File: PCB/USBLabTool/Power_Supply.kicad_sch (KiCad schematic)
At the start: 53 parts, among them J19 T_N5V, U10 Opamp_Quad, U11 DG403, U13 r1283, U15 ST1L05APU33R, U16 LTC1983ES6-5#TRPBF, U19 ST1L05APU33R, U9 Opamp_Quad

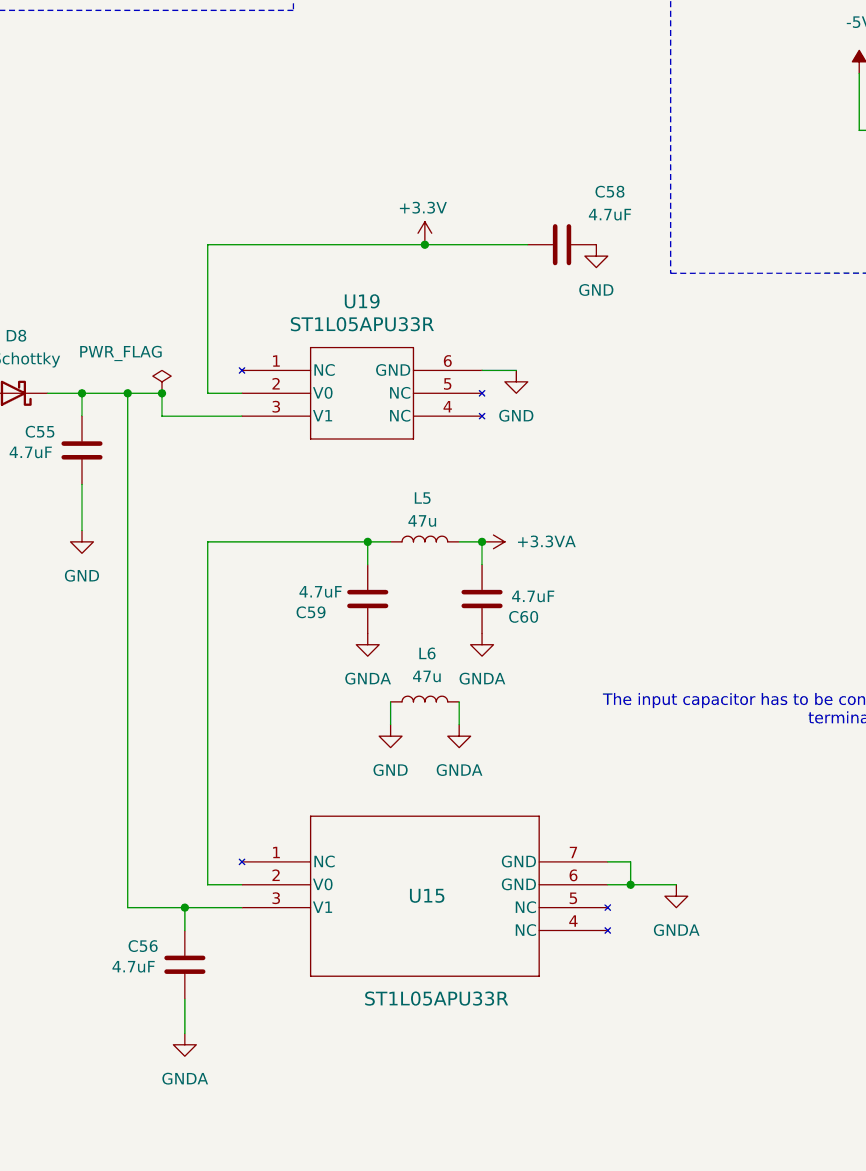
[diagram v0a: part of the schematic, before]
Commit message: update ST1L05APU33R schematic
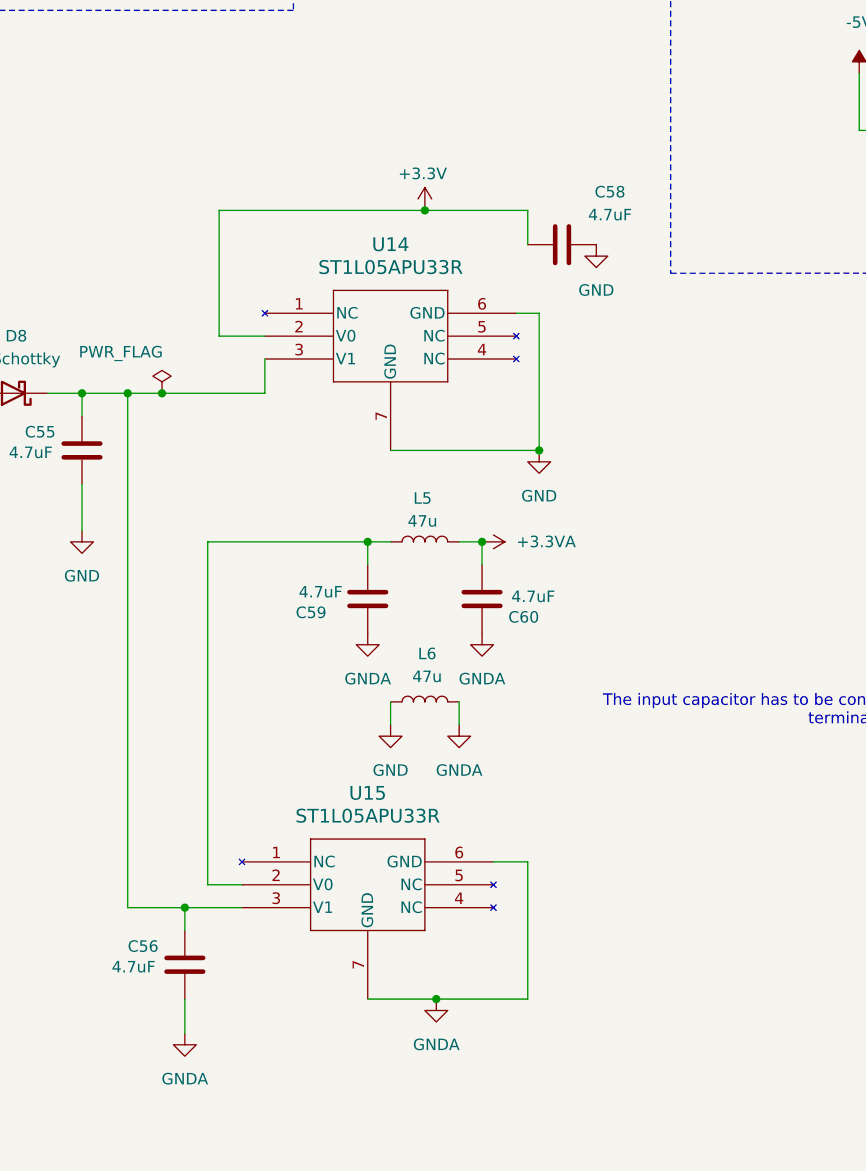
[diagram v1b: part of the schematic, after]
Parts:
- removed U15: ST1L05APU33R, DFN_5APU33R_STM, symbol ST1L05APU33R:ST1L05APU33R
- removed U19: ST1L05APU33R, DFN_5APU33R_STM, symbol USBLabTool:ST1L05APU33R
- added U14, U15: ST1L05APU33R, DFN_5APU33R_STM, symbol USBLabTool:ST1L05APU33R
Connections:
- net +3.3V: now also U14.2 (V0)
- net GND: now also U14.6 (GND), U14.7 (GND)
- net GNDA: now also U15.6 (GND), U15.7 (GND)
- net at C59.2, L5.1: now also U15.2 (V0)
- net at C55.1, C56.1, D8.1 (K): now also U14.3 (V1), U15.3 (V1)

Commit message: continue PCB layout
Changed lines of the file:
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@@
 (kicad_sch
-	(version 20231120)
+	(version 20250114)
 	(generator "eeschema")
-	(generator_version "8.0")
+	(generator_version "9.0")
 	(paper "A4")
+	(rectangle
+		(start 117.475 19.05)
+		(end 151.765 53.975)
+		(stroke
+			(width 0)
+			(type dash)
+		)
+		(fill
+			(type none)
+		)
+	)
+	(text "R1283K002A"
+		(exclude_from_sim no)
+		(at 29.21 95.25 0)
+		(effects
+			(font
+				(size 1.27 1.27)
+			)
+			(justify left bottom)
+		)
+	)
+	(text "Rf"
+		(exclude_from_sim no)
+		(at 64.135 94.615 0)
+		(effects
+			(font
+				(size 1.27 1.27)
+			)
+			(justify left bottom)
+		)
+	)
+	(text "The input capacitor has to be connected within 1 cm from VI\n terminal."
+		(exclude_from_sim no)
+		(at 212.598 131.826 0)
+		(effects
+			(font
+				(size 1.27 1.27)
+			)
+		)
+	)
+	(text "https://climbers.net/sbc/dual-rail-12v-dcdc-converter/"
+		(exclude_from_sim no)
+		(at 60.96 67.31 0)
+		(effects
+			(font
+				(size 1.27 1.27)
+			)
+			(justify left bottom)
+		)
+	)
+	(text "Add this near VDDA pin"
+		(exclude_from_sim no)
+		(at 138.938 25.654 0)
+		(effects
+			(font
+				(size 1.27 1.27)
+			)
+		)
+	)
+	(text "V=(Rg+Rf)/Rg"
+		(exclude_from_sim no)
+		(at 73.025 81.28 0)
+		(effects
+			(font
+				(size 1.27 1.27)
+			)
+			(justify left bottom)
+		)
+	)
+	(text "V=-1.2(Rf/Rr)"
+		(exclude_from_sim no)
+		(at 88.265 108.585 0)
+		(effects
+			(font
+				(size 1.27 1.27)
+			)
+			(justify right bottom)
+		)
+	)
+	(text "Rg"
+		(exclude_from_sim no)
+		(at 75.565 99.06 0)
+		(effects
+			(font
+				(size 1.27 1.27)
+			)
+			(justify left bottom)
+		)
+	)
+	(text "Negative 5V Power supply"
+		(exclude_from_sim no)
+		(at 179.6288 19.9136 0)
+		(effects
+			(font
+				(size 1.27 1.27)
+				(thickness 0.254)
+				(bold yes)
+			)
+			(justify left bottom)
+		)
+	)
+	(text "Rf"
+		(exclude_from_sim no)
+		(at 58.42 119.38 0)
+		(effects
+			(font
+				(size 1.27 1.27)
+			)
+			(justify left bottom)
+		)
+	)
+	(text "Rr"
+		(exclude_from_sim no)
+		(at 67.31 136.525 0)
+		(effects
+			(font
+				(size 1.27 1.27)
+			)
+			(justify left bottom)
+		)
+	)
 	(junction
 		(at 231.14 67.31)
@@
 		)
 	)
-	(rectangle
-		(start 117.475 19.05)
-		(end 151.765 53.975)
-		(stroke
-			(width 0)
-			(type dash)
-		)
-		(fill
-			(type none)
-		)
-	)
-	(text "R1283K002A"
-		(exclude_from_sim no)
-		(at 29.21 95.25 0)
-		(effects
-			(font
-				(size 1.27 1.27)
-			)
-			(justify left bottom)
-		)
-	)
-	(text "Rf"
-		(exclude_from_sim no)
-		(at 64.135 94.615 0)
-		(effects
-			(font
-				(size 1.27 1.27)
-			)
-			(justify left bottom)
-		)
-	)
-	(text "The input capacitor has to be connected within 1 cm from VI\n terminal."
-		(exclude_from_sim no)
-		(at 212.598 131.826 0)
-		(effects
-			(font
-				(size 1.27 1.27)
-			)
-		)
-	)
-	(text "https://climbers.net/sbc/dual-rail-12v-dcdc-converter/"
-		(exclude_from_sim no)
-		(at 60.96 67.31 0)
-		(effects
-			(font
-				(size 1.27 1.27)
-			)
-			(justify left bottom)
-		)
-	)
-	(text "Add this near VDDA pin"
-		(exclude_from_sim no)
-		(at 138.938 25.654 0)
-		(effects
-			(font
-				(size 1.27 1.27)
-			)
-		)
-	)
-	(text "V=(Rg+Rf)/Rg"
-		(exclude_from_sim no)
-		(at 73.025 81.28 0)
-		(effects
-			(font
-				(size 1.27 1.27)
-			)
-			(justify left bottom)
-		)
-	)
-	(text "V=-1.2(Rf/Rr)"
-		(exclude_from_sim no)
-		(at 88.265 108.585 0)
-		(effects
-			(font
-				(size 1.27 1.27)
-			)
-			(justify right bottom)
-		)
-	)
-	(text "Rg"
-		(exclude_from_sim no)
-		(at 75.565 99.06 0)
-		(effects
-			(font
-				(size 1.27 1.27)
-			)
-			(justify left bottom)
-		)
-	)
-	(text "Negative 5V Power supply"
-		(exclude_from_sim no)
-		(at 179.6288 19.9136 0)
-		(effects
-			(font
-				(size 1.27 1.27)
-				(thickness 0.254)
-				(bold yes)
-			)
-			(justify left bottom)
-		)
-	)
-	(text "Rf"
-		(exclude_from_sim no)
-		(at 58.42 119.38 0)
-		(effects
-			(font
-				(size 1.27 1.27)
-			)
-			(justify left bottom)
-		)
-	)
-	(text "Rr"
-		(exclude_from_sim no)
-		(at 67.31 136.525 0)
-		(effects
-			(font
-				(size 1.27 1.27)
-			)
-			(justify left bottom)
-		)
-	)
 	(symbol
 		(lib_id "Device:C")
@@
 		)
 	)
+	(embedded_fonts no)
 )

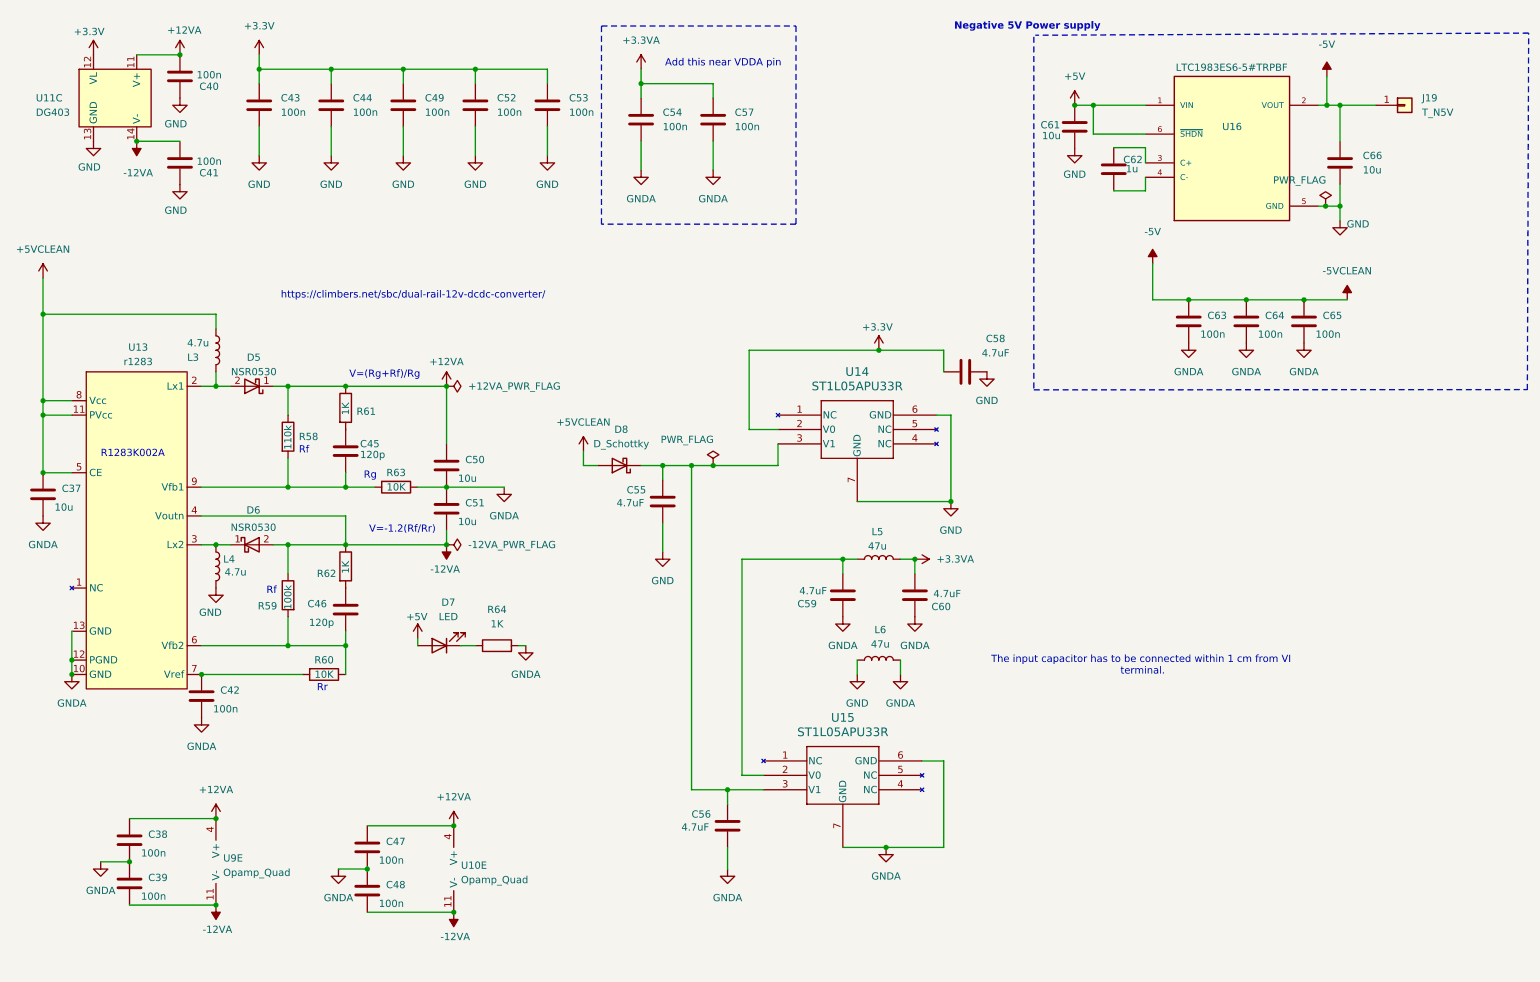
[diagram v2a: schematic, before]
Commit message: fixed grounds for several components and fix 5V clean
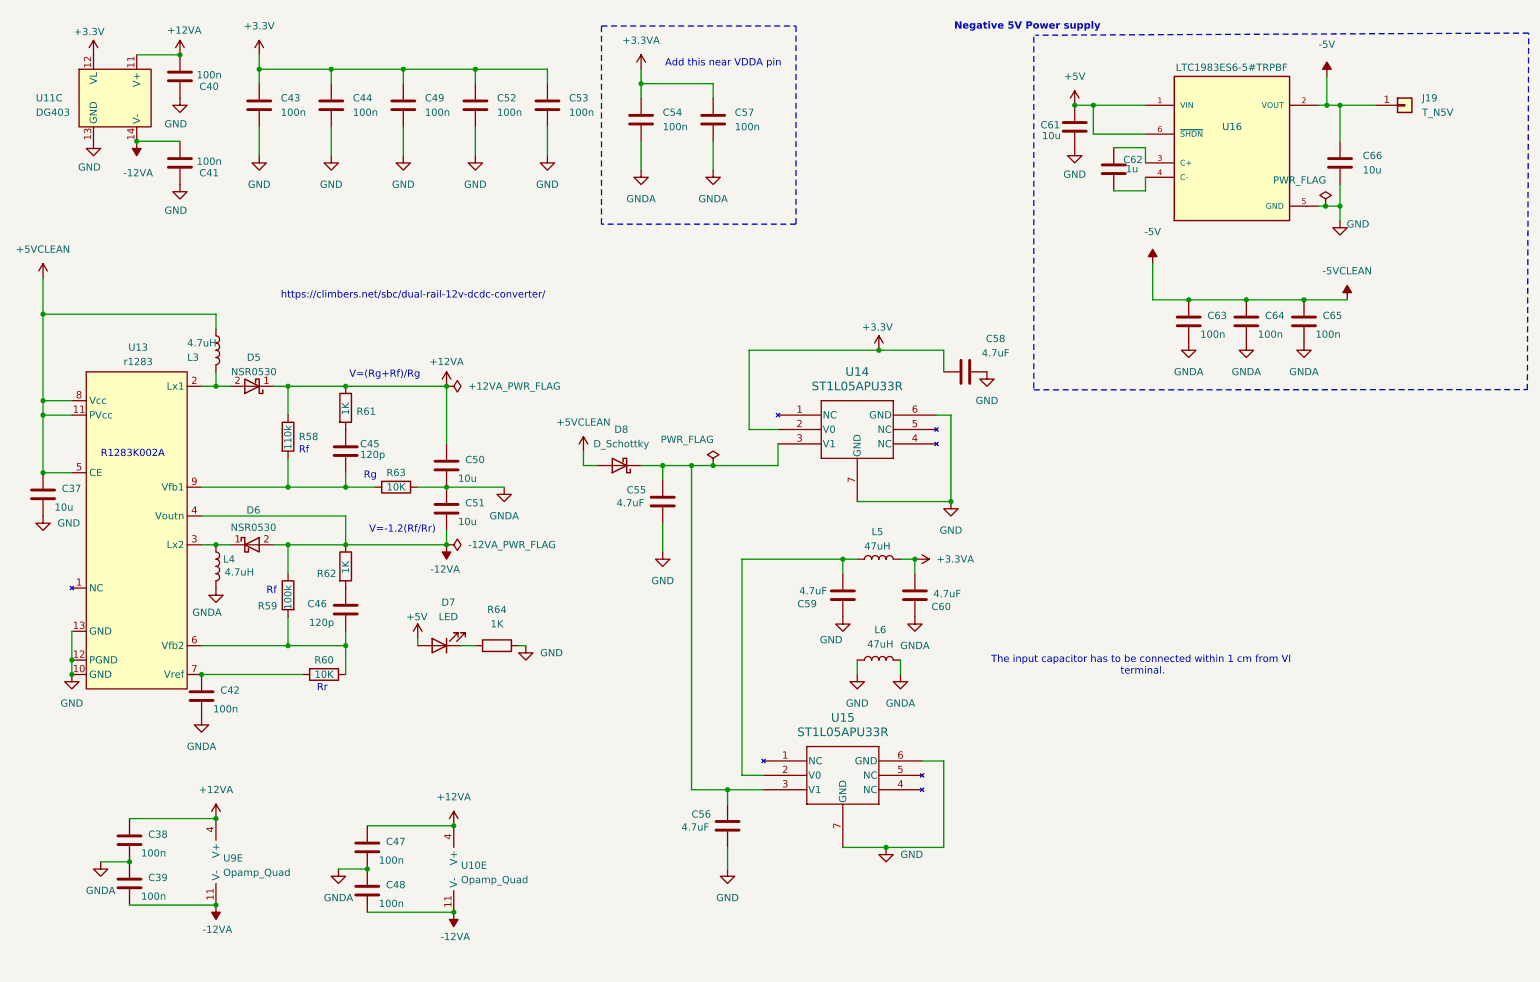
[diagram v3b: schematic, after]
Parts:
- L3, L4: value 4.7u -> 4.7uH
- L5, L6: value 47u -> 47uH
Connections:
- net GND: now also C37.2, C56.2, C59.1, R64.2, U13.10 (GND), U13.12 (PGND), U13.13 (GND), U15.6 (GND), U15.7 (GND); no longer L4.2
- net GNDA: now also L4.2; no longer C37.2, C56.2, C59.1, R64.2, U13.10 (GND), U13.12 (PGND), U13.13 (GND), U15.6 (GND), U15.7 (GND)
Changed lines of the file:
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@@
 			)
 		)
-		(property "Value" "47u"
+		(property "Value" "47uH"
 			(at 166.624 128.016 90)
 			(effects
@@
 		(on_board yes)
 		(dnp no)
-		(fields_autoplaced yes)
 		(property "Reference" "#PWR0116"
 			(at 160.02 129.54 0)
@@
 			)
 		)
-		(property "Value" "GNDA"
-			(at 160.02 128.27 0)
+		(property "Value" "GND"
+			(at 155.956 127.254 0)
 			(effects
 				(font
 					(size 1.27 1.27)
 				)
+				(justify left)
 			)
 		)
@@
 		(on_board yes)
 		(dnp no)
-		(fields_autoplaced yes)
 		(property "Reference" "#PWR0106"
 			(at 114.3 97.79 0)
@@
 			)
 		)
-		(property "Value" "GNDA"
+		(property "Value" "GND"
 			(at 139.7 172.72 0)
 			(effects
@@
 			)
 		)
-		(property "Value" "GNDA"
-			(at 104.14 133.35 0)
+		(property "Value" "GND"
+			(at 106.68 129.5399 0)
 			(effects
 				(font
 					(size 1.27 1.27)
 				)
+				(justify left)
 			)
 		)
@@
 			)
 		)
-		(property "Value" "4.7u"
+		(property "Value" "4.7uH"
 			(at 44.45 74.93 0)
 			(effects
@@
 			)
 		)
-		(property "Value" "4.7u"
+		(property "Value" "4.7uH"
 			(at 51.054 115.316 0)
 			(effects
@@
 			)
 		)
-		(property "Value" "GND"
+		(property "Value" "GNDA"
 			(at 50.546 122.428 0)
 			(effects
@@
 			)
 		)
-		(property "Value" "GNDA"
-			(at 19.05 110.49 0)
+		(property "Value" "GND"
+			(at 21.59 106.6799 0)
 			(effects
 				(font
 					(size 1.27 1.27)
 				)
+				(justify left)
 			)
 		)
@@
 			)
 		)
-		(property "Value" "47u"
+		(property "Value" "47uH"
 			(at 166.116 110.744 90)
 			(effects
@@
 			)
 		)
-		(property "Value" "GNDA"
-			(at 167.64 168.91 0)
+		(property "Value" "GND"
+			(at 170.18 165.0999 0)
 			(effects
 				(font
 					(size 1.27 1.27)
 				)
+				(justify left)
 			)
 		)
@@
 		(on_board yes)
 		(dnp no)
-		(fields_autoplaced yes)
 		(property "Reference" "#PWR080"
 			(at 24.13 139.7 0)
@@
 			)
 		)
-		(property "Value" "GNDA"
+		(property "Value" "GND"
 			(at 24.13 138.43 0)
 			(effects

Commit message: final version prototype
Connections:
- net +5VCLEAN is gone; now on net +5V: C37.1, D8.2 (A), L3.1, U13.11 (PVcc), U13.5 (CE), U13.8 (Vcc)
- net GND: now also C42.2, L4.2
- net GNDA: no longer C42.2, L4.2

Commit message: fix footprint and change button
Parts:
- U10, U9: footprint Package_SO:SOIC-14W_7.5x9mm_P1.27mm -> Package_SO:SOIC-14_3.9x8.7mm_P1.27mm
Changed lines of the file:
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@@
 			)
 		)
-		(property "Footprint" "Package_SO:SOIC-14W_7.5x9mm_P1.27mm"
+		(property "Footprint" "Package_SO:SOIC-14_3.9x8.7mm_P1.27mm"
 			(at 52.07 166.37 0)
 			(effects
@@
 			)
 		)
+		(property "Purpose" ""
+			(at 52.07 166.37 0)
+			(effects
+				(font
+					(size 1.27 1.27)
+				)
+				(hide yes)
+			)
+		)
 		(pin "1"
 		)
@@
 			)
 		)
-		(property "Footprint" "Package_SO:SOIC-14W_7.5x9mm_P1.27mm"
+		(property "Footprint" "Package_SO:SOIC-14_3.9x8.7mm_P1.27mm"
 			(at 93.98 167.64 0)
 			(effects
@@
 			(at 93.98 167.64 0)
 			(effects
+				(font
+					(size 1.27 1.27)
+				)
+				(hide yes)
+			)
+		)
+		(property "Purpose" ""
+			(at 93.98 167.64 0)
+			(effects

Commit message: change USB footprint, fix some warnings and problems
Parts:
- U14, U15: footprint DFN_5APU33R_STM -> userfp:DFN_5APU33R_STM
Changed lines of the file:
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@@
 			)
 		)
-		(property "Footprint" "DFN_5APU33R_STM"
+		(property "Footprint" "userfp:DFN_5APU33R_STM"
 			(at 146.05 151.13 0)
 			(effects
@@
 			)
 		)
-		(property "Footprint" "DFN_5APU33R_STM"
+		(property "Footprint" "userfp:DFN_5APU33R_STM"
 			(at 148.59 90.17 0)
 			(effects
